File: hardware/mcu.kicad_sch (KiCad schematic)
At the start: 13 parts, among them J1 Micro_SD_Card, J2 Conn_01x40, J3 USB_C_Receptacle_USB2.0_14P, U1 ESP32-S3-WROOM-1

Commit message: add lcd sch
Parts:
- removed J2: Conn_01x40, Connector_FFC-FPC:Hirose_FH12-40S-0.5SH_1x40-1MP_P0.50mm_Horizontal, symbol Connector_Generic:Conn_01x40
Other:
- moved on the sheet: U1
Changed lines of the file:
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@@
 	(symbol
 		(lib_id "RF_Module:ESP32-S3-WROOM-1")
-		(at 44.45 60.96 0)
+		(at 86.36 66.04 0)
 		(unit 1)
 		(exclude_from_sim no)
@@
 		(fields_autoplaced yes)
 		(property "Reference" "U1"
-			(at 46.6441 30.48 0)
+			(at 88.5541 35.56 0)
 			(effects
 				(font
@@
 		)
 		(property "Value" "ESP32-S3-WROOM-1"
-			(at 46.6441 33.02 0)
+			(at 88.5541 38.1 0)
 			(effects
 				(font
@@
 		)
 		(property "Footprint" "RF_Module:ESP32-S3-WROOM-1"
-			(at 44.45 58.42 0)
+			(at 86.36 63.5 0)
 			(effects
 				(font
@@
 		)
 		(property "Datasheet" "https://www.espressif.com/sites/default/files/documentation/esp32-s3-wroom-1_wroom-1u_datasheet_en.pdf"
-			(at 44.45 60.96 0)
+			(at 86.36 66.04 0)
 			(effects
 				(font
@@
 		)
 		(property "Description" "RF Module, ESP32-S3 SoC, Wi-Fi 802.11b/g/n, Bluetooth, BLE, 32-bit, 3.3V, onboard antenna, SMD"
-			(at 44.45 60.96 0)
+			(at 86.36 66.04 0)
 			(effects
 				(font
@@
 					(unit 1)
 				)
-			)
-		)
-	)
-	(symbol
-		(lib_id "Connector_Generic:Conn_01x40")
-		(at 91.44 71.12 0)
-		(unit 1)
-		(exclude_from_sim no)
-		(in_bom yes)
-		(on_board yes)
-		(dnp no)
-		(fields_autoplaced yes)
-		(property "Reference" "J2"
-			(at 93.98 71.1199 0)
-			(effects
-				(font
-					(size 1.27 1.27)
-				)
-				(justify left)
-			)
-		)
-		(property "Value" "Conn_01x40"
-			(at 93.98 73.6599 0)
-			(effects
-				(font
-					(size 1.27 1.27)
-				)
-				(justify left)
-			)
-		)
-		(property "Footprint" "Connector_FFC-FPC:Hirose_FH12-40S-0.5SH_1x40-1MP_P0.50mm_Horizontal"
-			(at 91.44 71.12 0)
-			(effects
-				(font
-					(size 1.27 1.27)
-				)
-				(hide yes)
-			)
-		)
-		(property "Datasheet" "~"
-			(at 91.44 71.12 0)
-			(effects
-				(font
-					(size 1.27 1.27)
-				)
-				(hide yes)
-			)
-		)
-		(property "Description" "Generic connector, single row, 01x40, script generated (kicad-library-utils/schlib/autogen/connector/)"
-			(at 91.44 71.12 0)
-			(effects
-				(font
-					(size 1.27 1.27)
-				)
-				(hide yes)
-			)
-		)
-		(pin "30"
-		)
-		(pin "25"
-		)
-		(pin "34"
-		)
-		(pin "12"
-		)
-		(pin "27"
-		)
-		(pin "26"
-		)
-		(pin "33"
-		)
-		(pin "28"
-		)
-		(pin "11"
-		)
-		(pin "1"
-		)
-		(pin "10"
-		)
-		(pin "37"
-		)
-		(pin "13"
-		)
-		(pin "35"
-		)
-		(pin "40"
-		)
-		(pin "15"
-		)
-		(pin "8"
-		)
-		(pin "38"
-		)
-		(pin "2"
-		)
-		(pin "20"
-		)
-		(pin "17"
-		)
-		(pin "18"
-		)
-		(pin "31"
-		)
-		(pin "39"
-		)
-		(pin "5"
-		)
-		(pin "29"
-		)
-		(pin "36"
-		)
-		(pin "16"
-		)
-		(pin "21"
-		)
-		(pin "22"
-		)
-		(pin "6"
-		)
-		(pin "19"
-		)
-		(pin "14"
-		)
-		(pin "32"
-		)
-		(pin "24"
-		)
-		(pin "7"
-		)
-		(pin "3"
-		)
-		(pin "23"
-		)
-		(pin "9"
-		)
-		(pin "4"
-		)
-		(instances
-			(project "badge"
-				(path "/dc4a3d77-b0f8-4e90-a4be-3e93c7025348/d3fb9833-a00e-444d-9e5a-c108fd26b22a"
-					(reference "J2")
-					(unit 1)
-				)

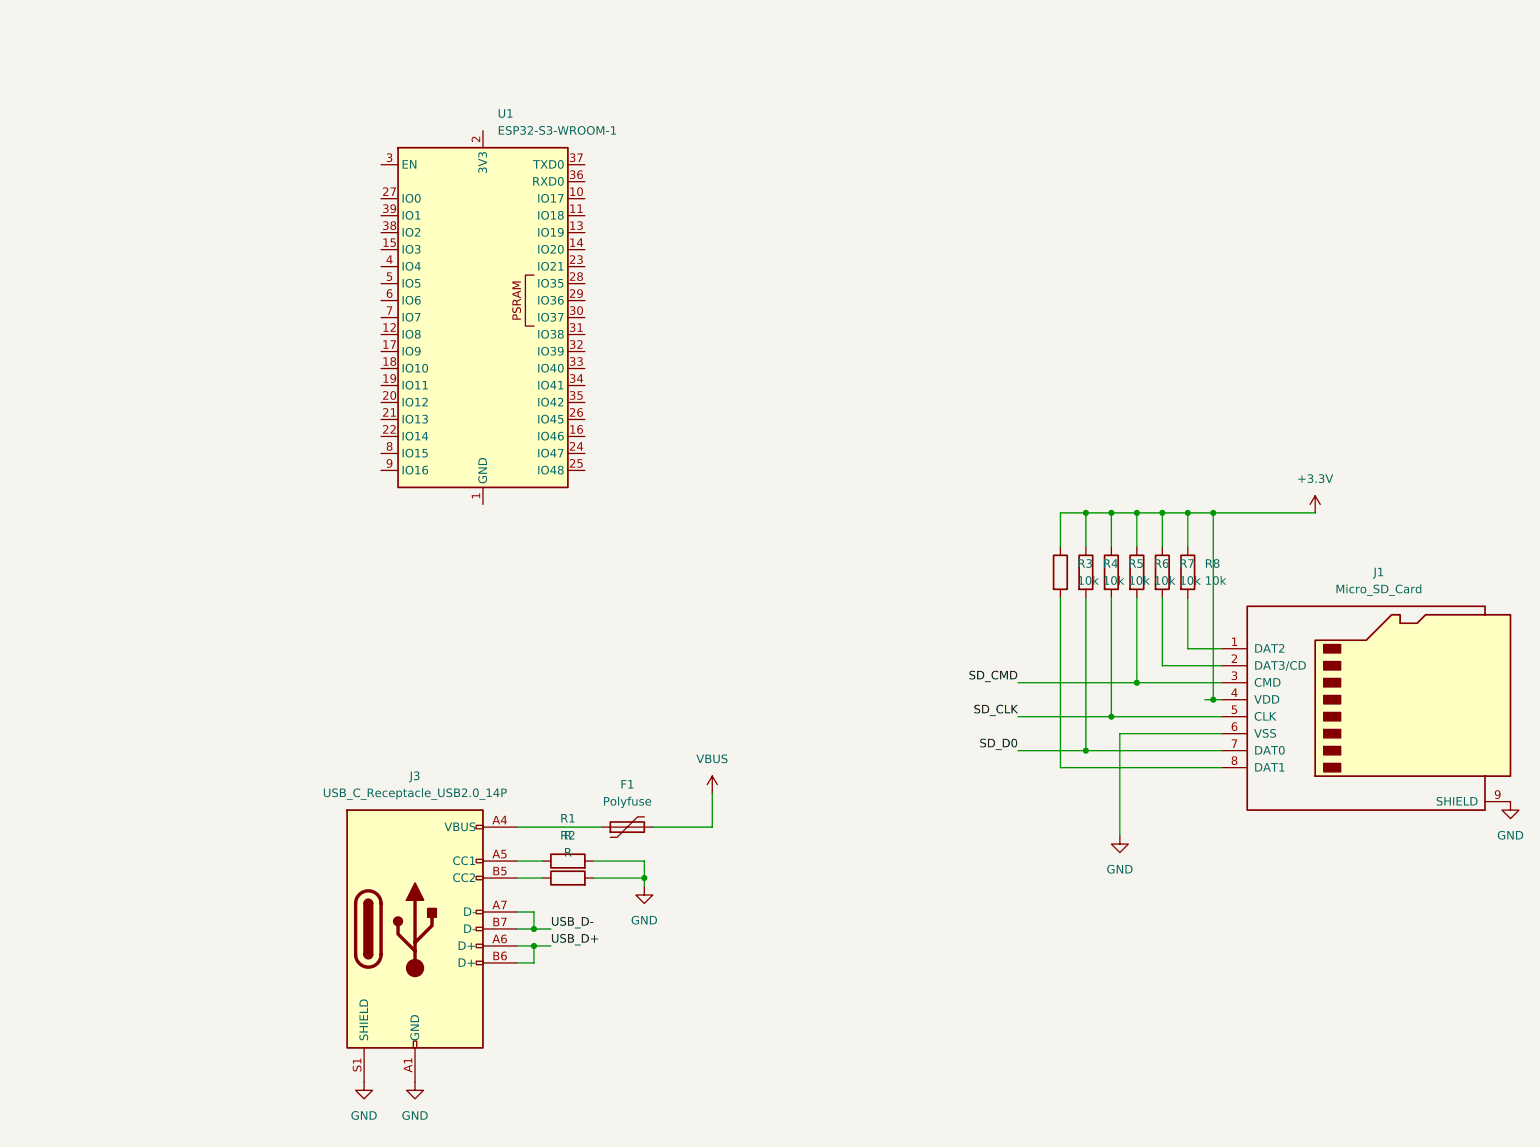
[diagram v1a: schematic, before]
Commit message: add ch340g
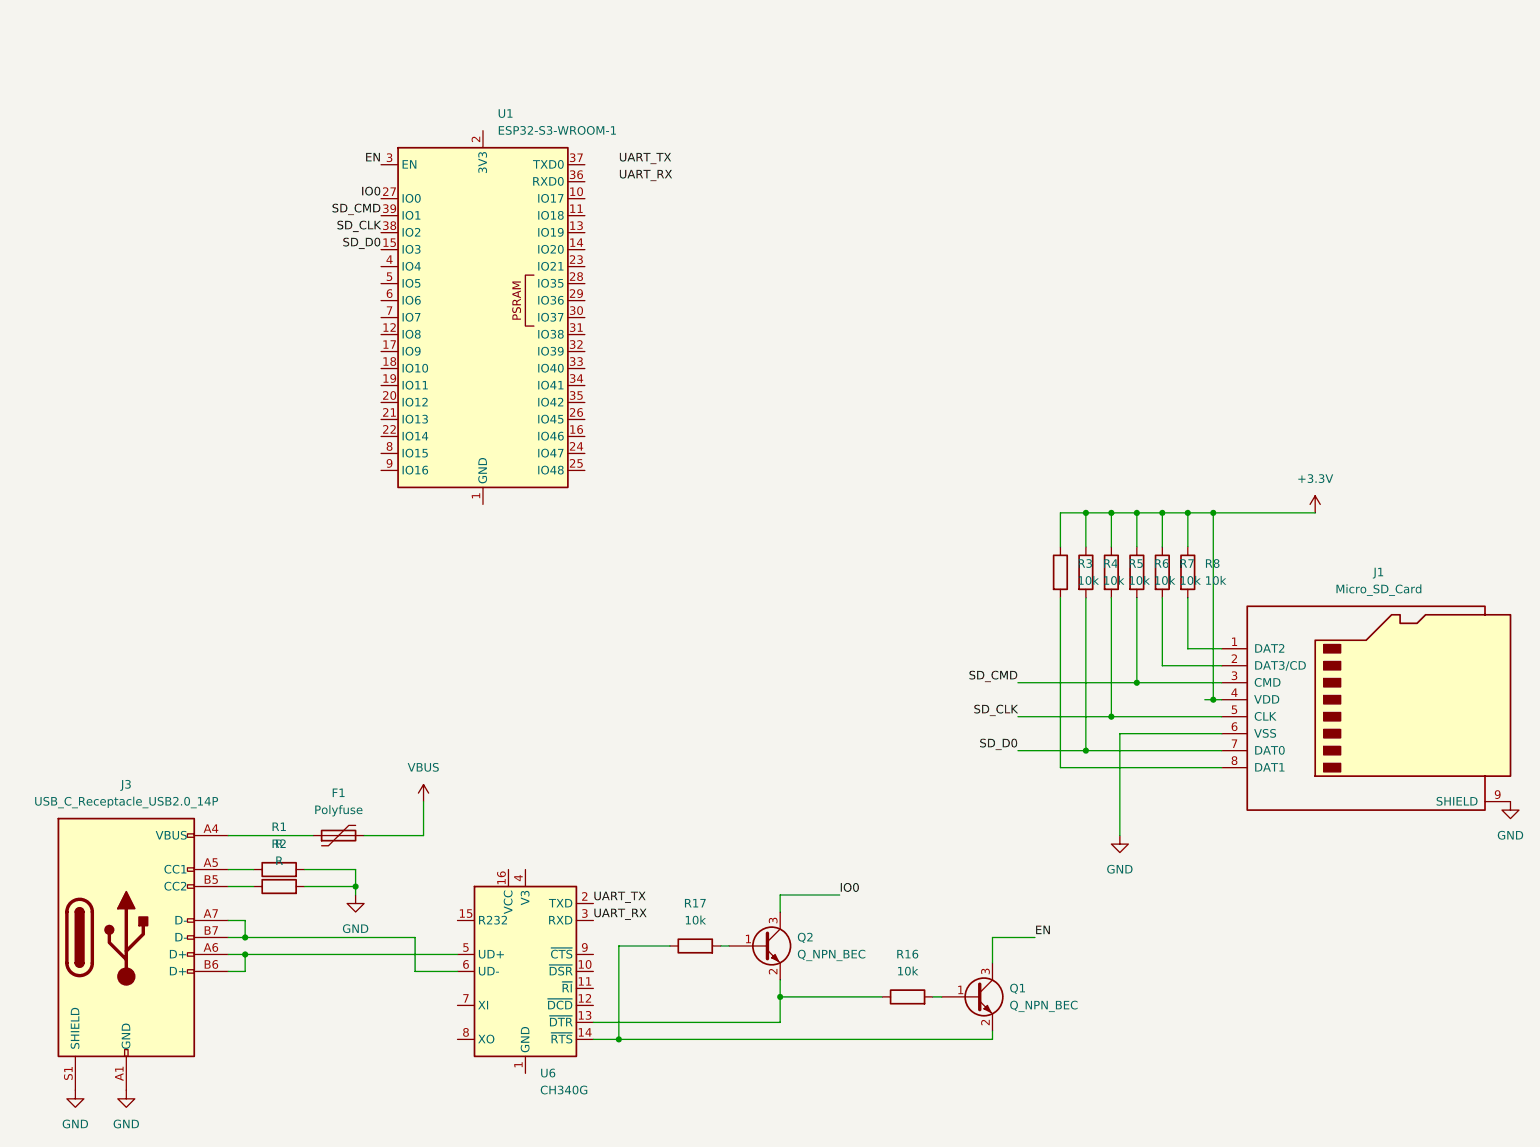
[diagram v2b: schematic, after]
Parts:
- added Q1, Q2: Q_NPN_BEC, symbol Device:Q_NPN_BEC
- added R16, R17: 10k, symbol Device:R
- added U6: CH340G, Package_SO:SOIC-16_3.9x9.9mm_P1.27mm, symbol Interface_USB:CH340G
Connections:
- net SD_CLK: now also U1.38 (IO2)
- net SD_CMD: now also U1.39 (IO1)
- net SD_D0: now also U1.15 (IO3)
- net IO0: now reaches U1.27 (IO0)
- net IO0: now also Q2.3 (C)
- net EN: now reaches U1.3 (EN)
- net EN: now also Q1.3 (C)
- net USB_D+: no longer names the net of J3.A6 (D+), J3.B6 (D+)
- net USB_D+: now also U6.5 (UD+)
- net USB_D-: no longer names the net of J3.A7 (D-), J3.B7 (D-)
- net USB_D-: now also U6.6 (UD-)
- new net: Q1.2 (E), R17.1, U6.14 (~{RTS})
- new net: Q2.1 (B), R17.2
- new net: Q2.2 (E), R16.1, U6.13 (~{DTR})
- new net: Q1.1 (B), R16.2
- new net UART_RX: U6.3 (RXD)
- new net UART_TX: U6.2 (TXD)
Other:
- moved on the sheet: F1, J3, R1, R2

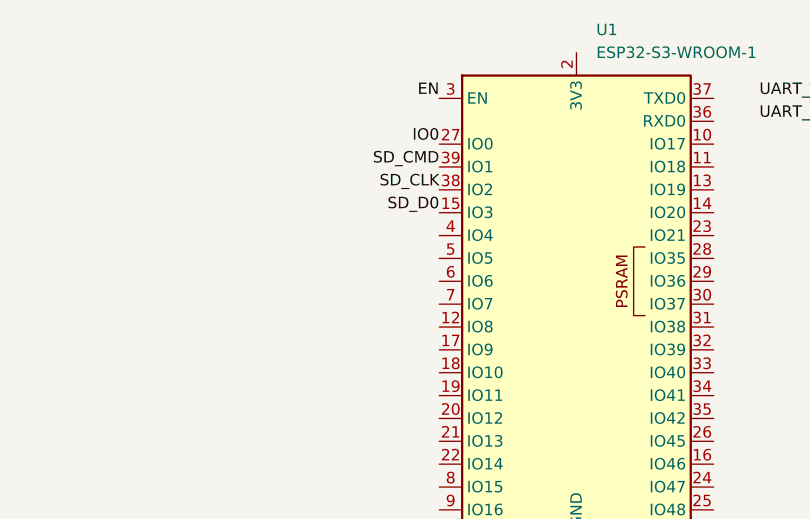
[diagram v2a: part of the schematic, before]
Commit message: chg pin
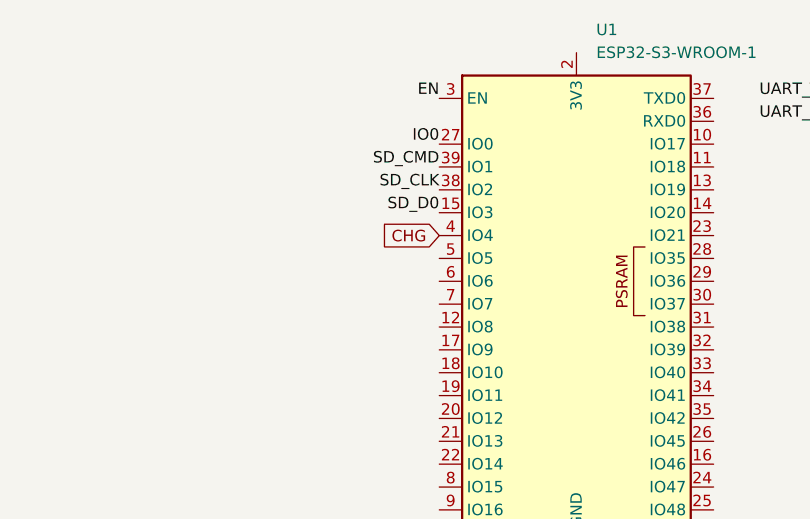
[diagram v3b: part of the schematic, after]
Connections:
- net CHG: now reaches U1.4 (IO4)
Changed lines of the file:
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@@
+		)
+	)
+	(global_label "CHG"
+		(shape input)
+		(at 71.12 58.42 180)
+		(fields_autoplaced yes)
+		(effects
+			(font
+				(size 1.27 1.27)
+			)
+			(justify right)
+		)
+		(property "Intersheetrefs" "${INTERSHEET_REFS}"
+			(at 64.2643 58.42 0)
+			(effects
+				(font
+					(size 1.27 1.27)
+				)
+				(justify right)
+				(hide yes)
+			)
 		)
 	)

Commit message: fix ch340
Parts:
- added R21, R22: 100, Resistor_SMD:R_0201_0603Metric, symbol Device:R
- R1, R2: value R -> TBD
- U6: LCSC (none) -> C14267
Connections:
- net +3.3V: now also U6.4 (V3)
- net GND: now also U6.1 (GND)
- net VBUS: now also U6.16 (VCC)
- net at J3.A6 (D+), J3.B6 (D+): now also R22.1; no longer U6.5 (UD+)
- net at J3.A7 (D-), J3.B7 (D-): now also R21.1; no longer U6.6 (UD-)
- new net: R22.2, U6.5 (UD+)
- new net: R21.2, U6.6 (UD-)

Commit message: keyboard schematic
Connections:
- net KB_COL0: now reaches U1.12 (IO8)
- net KB_COL1: now reaches U1.17 (IO9)
- net KB_COL2: now reaches U1.18 (IO10)
- net KB_COL3: now reaches U1.19 (IO11)
- net KB_COL4: now reaches U1.20 (IO12)
- net KB_COL5: now reaches U1.21 (IO13)
- net KB_COL6: now reaches U1.22 (IO14)
- net KB_ROW0: now reaches U1.5 (IO5)
- net KB_ROW1: now reaches U1.6 (IO6)
- net KB_ROW2: now reaches U1.7 (IO7)
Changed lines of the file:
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@@
+		)
+	)
+	(global_label "KB_ROW0"
+		(shape input)
+		(at 71.12 60.96 180)
+		(fields_autoplaced yes)
+		(effects
+			(font
+				(size 1.27 1.27)
+			)
+			(justify right)
+		)
+		(property "Intersheetrefs" "${INTERSHEET_REFS}"
+			(at 59.3658 60.96 0)
+			(effects
+				(font
+					(size 1.27 1.27)
+				)
+				(justify right)
+				(hide yes)
+			)
+		)
+	)
+	(global_label "KB_COL0"
+		(shape input)
+		(at 71.12 68.58 180)
+		(fields_autoplaced yes)
+		(effects
+			(font
+				(size 1.27 1.27)
+			)
+			(justify right)
+		)
+		(property "Intersheetrefs" "${INTERSHEET_REFS}"
+			(at 59.7891 68.58 0)
+			(effects
+				(font
+					(size 1.27 1.27)
+				)
+				(justify right)
+				(hide yes)
+			)
+		)
+	)
+	(global_label "KB_ROW1"
+		(shape input)
+		(at 71.12 63.5 180)
+		(fields_autoplaced yes)
+		(effects
+			(font
+				(size 1.27 1.27)
+			)
+			(justify right)
+		)
+		(property "Intersheetrefs" "${INTERSHEET_REFS}"
+			(at 59.3658 63.5 0)
+			(effects
+				(font
+					(size 1.27 1.27)
+				)
+				(justify right)
+				(hide yes)
+			)
 		)
 	)
@@
 			(effects
 				(font
+					(size 1.27 1.27)
+				)
+				(justify right)
+				(hide yes)
+			)
+		)
+	)
+	(global_label "KB_COL1"
+		(shape input)
+		(at 71.12 71.12 180)
+		(fields_autoplaced yes)
+		(effects
+			(font
+				(size 1.27 1.27)
+			)
+			(justify right)
+		)
+		(property "Intersheetrefs" "${INTERSHEET_REFS}"
+			(at 59.7891 71.12 0)
+			(effects
+				(font
+					(size 1.27 1.27)
+				)
+				(justify right)
+				(hide yes)
+			)
+		)
+	)
+	(global_label "KB_COL4"
+		(shape input)
+		(at 71.12 78.74 180)
+		(fields_autoplaced yes)
+		(effects
+			(font
+				(size 1.27 1.27)
+			)
+			(justify right)
+		)
+		(property "Intersheetrefs" "${INTERSHEET_REFS}"
+			(at 59.7891 78.74 0)
+			(effects
+				(font
+					(size 1.27 1.27)
+				)
+				(justify right)
+				(hide yes)
+			)
+		)
+	)
+	(global_label "KB_COL2"
+		(shape input)
+		(at 71.12 73.66 180)
+		(fields_autoplaced yes)
+		(effects
+			(font
+				(size 1.27 1.27)
+			)
+			(justify right)
+		)
+		(property "Intersheetrefs" "${INTERSHEET_REFS}"
+			(at 59.7891 73.66 0)
+			(effects
+				(font
+					(size 1.27 1.27)
+				)
+				(justify right)
+				(hide yes)
+			)
+		)
+	)
+	(global_label "KB_COL5"
+		(shape input)
+		(at 71.12 81.28 180)
+		(fields_autoplaced yes)
+		(effects
+			(font
+				(size 1.27 1.27)
+			)
+			(justify right)
+		)
+		(property "Intersheetrefs" "${INTERSHEET_REFS}"
+			(at 59.7891 81.28 0)
+			(effects
+				(font
+					(size 1.27 1.27)
+				)
+				(justify right)
+				(hide yes)
+			)
+		)
+	)
+	(global_label "KB_COL6"
+		(shape input)
+		(at 71.12 83.82 180)
+		(fields_autoplaced yes)
+		(effects
+			(font
+				(size 1.27 1.27)
+			)
+			(justify right)
+		)
+		(property "Intersheetrefs" "${INTERSHEET_REFS}"
+			(at 59.7891 83.82 0)
+			(effects
+				(font
+					(size 1.27 1.27)
+				)
+				(justify right)
+				(hide yes)
+			)
+		)
+	)
+	(global_label "KB_ROW2"
+		(shape input)
+		(at 71.12 66.04 180)
+		(fields_autoplaced yes)
+		(effects
+			(font
+				(size 1.27 1.27)
+			)
+			(justify right)
+		)
+		(property "Intersheetrefs" "${INTERSHEET_REFS}"
+			(at 59.3658 66.04 0)
+			(effects
+				(font
+					(size 1.27 1.27)
+				)
+				(justify right)
+				(hide yes)
+			)
+		)
+	)
+	(global_label "KB_COL3"
+		(shape input)
+		(at 71.12 76.2 180)
+		(fields_autoplaced yes)
+		(effects
+			(font
+				(size 1.27 1.27)
+			)
+			(justify right)
+		)
+		(property "Intersheetrefs" "${INTERSHEET_REFS}"
+			(at 59.7891 76.2 0)
+			(effects
+				(font
